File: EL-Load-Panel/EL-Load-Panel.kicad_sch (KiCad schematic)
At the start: 40 parts, among them J2 Conn_02x08_Odd_Even, J3 Touchscreen, SW1 ON/OFF, U1 MCP23008-xSO

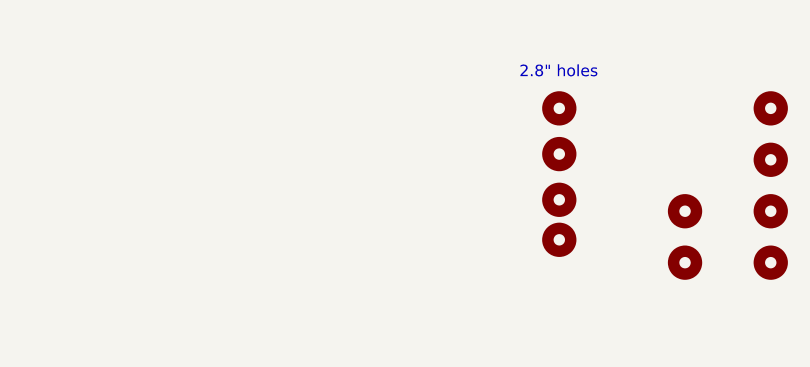
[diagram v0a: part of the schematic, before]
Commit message: Fixed Panel 1r1 and Power-MCU 2r2 versions
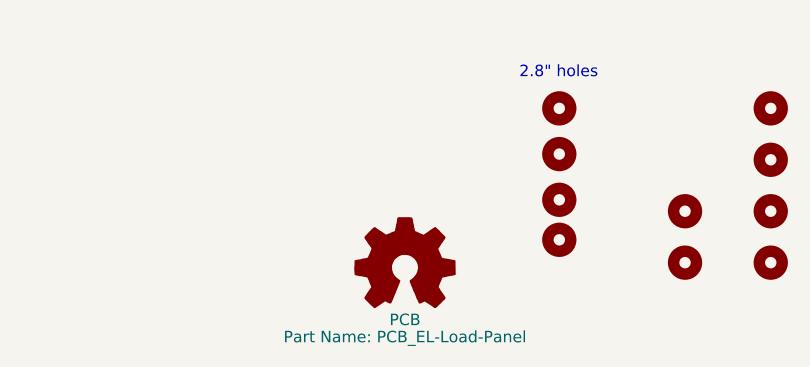
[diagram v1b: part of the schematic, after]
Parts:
- added PCB1: PCB, symbol Graphic:Logo_Open_Hardware_Small
- C1: Part Name (none) -> C_1.0uF_0805_20%
- C2: Part Name (none) -> C_100.0nF_50V_0805_10%
- C3, C4, C5, C7: Part Name (none) -> C_10.0nF_0805_20%
- D1: Part Name (none) -> D_LED_Rood_THT_3mm
- ENC1: Part Name (none) -> E_ENC_PEC11R-24D-20mm-Flat-24P
- J2: Part Name (none) -> H_IDC_2.54mm_Socket_THT_2x8pins
- J3: Consumable (none) -> 1; Part Name (none) -> H_Male_1x40_vertical_THT
- R1, R10, R12, R13, R2, R3, R4, R5, R6, R7, R8: Part Name (none) -> R_10.0kΩ_0805_1%
- R18: Part Name (none) -> R_270.0Ω_0805_1%
- SW1: Part Name (none) -> SW_SPST_NO_THT_6x6x10mm
- U1: Part Name (none) -> U_MCP23008-E/SO

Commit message: Updated EL-Load-Panel to 1r2, fixing issues in issue #3.
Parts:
- ENC1: footprint Rotary_Encoder:RotaryEncoder_Alps_EC12E-Switch_Vertical_H20mm -> Rotary_Encoder:RotaryEncoder_Bourns_Vertical_PEC12R-3x17F-Sxxxx
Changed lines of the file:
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@@
       (effects (font (size 1.27 1.27)) (justify left))
     )
-    (property "Footprint" "Rotary_Encoder:RotaryEncoder_Alps_EC12E-Switch_Vertical_H20mm" (at 171.069 53.34 0)
+    (property "Footprint" "Rotary_Encoder:RotaryEncoder_Bourns_Vertical_PEC12R-3x17F-Sxxxx" (at 171.069 53.34 0)
       (effects (font (size 1.27 1.27)) hide)
     )
